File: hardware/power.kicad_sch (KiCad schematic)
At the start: 27 parts, among them J3 Battery, U9 MCP73811T-420I-OT

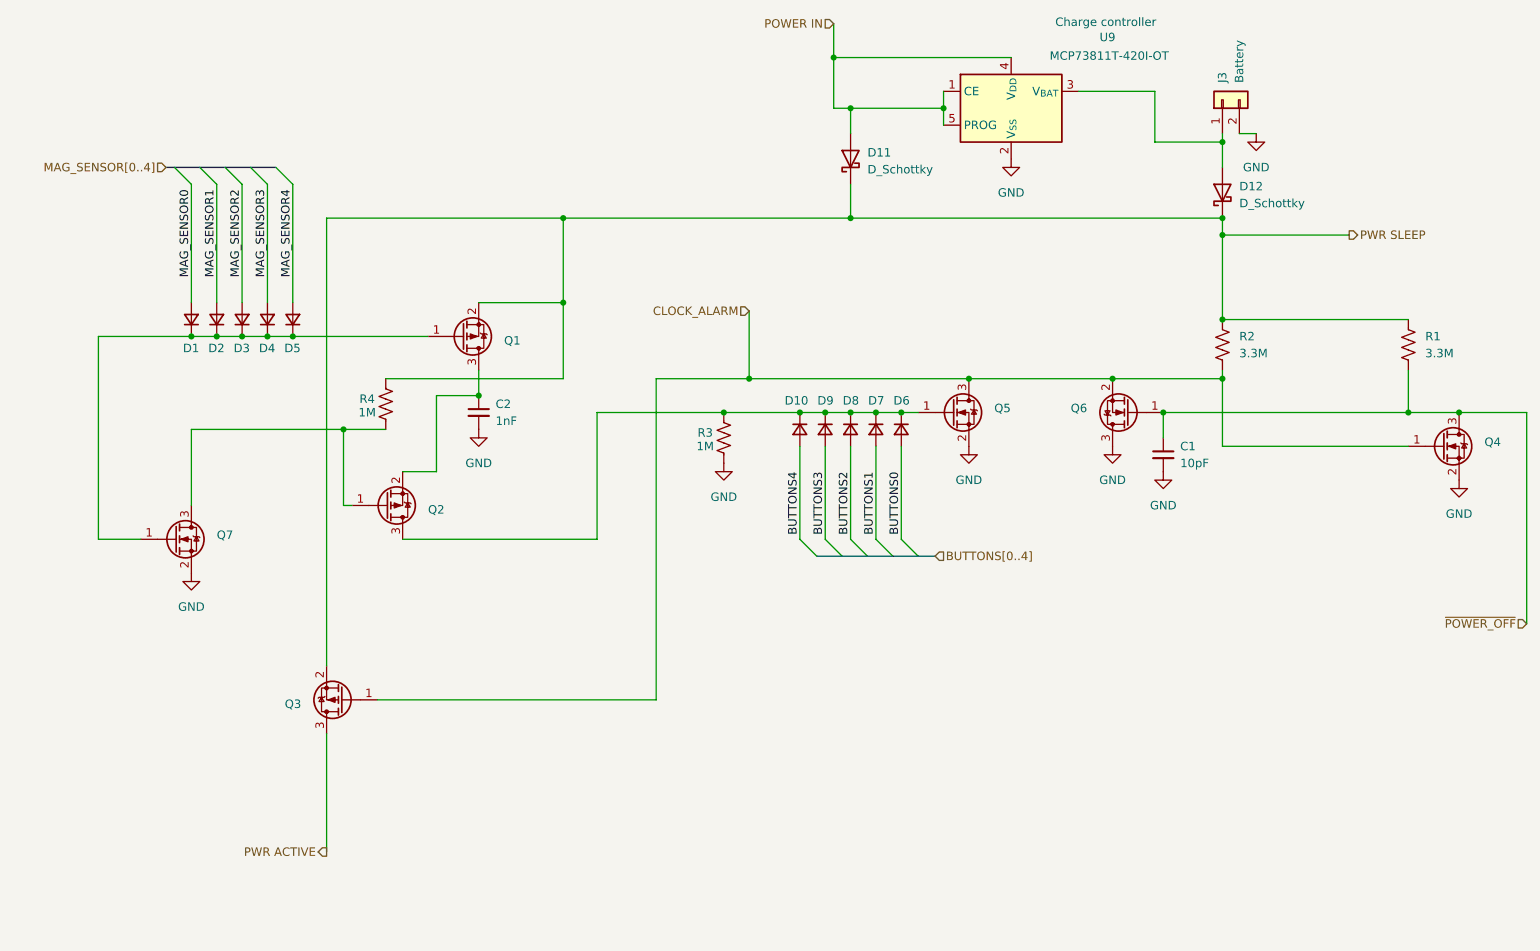
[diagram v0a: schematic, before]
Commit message: Schematic done
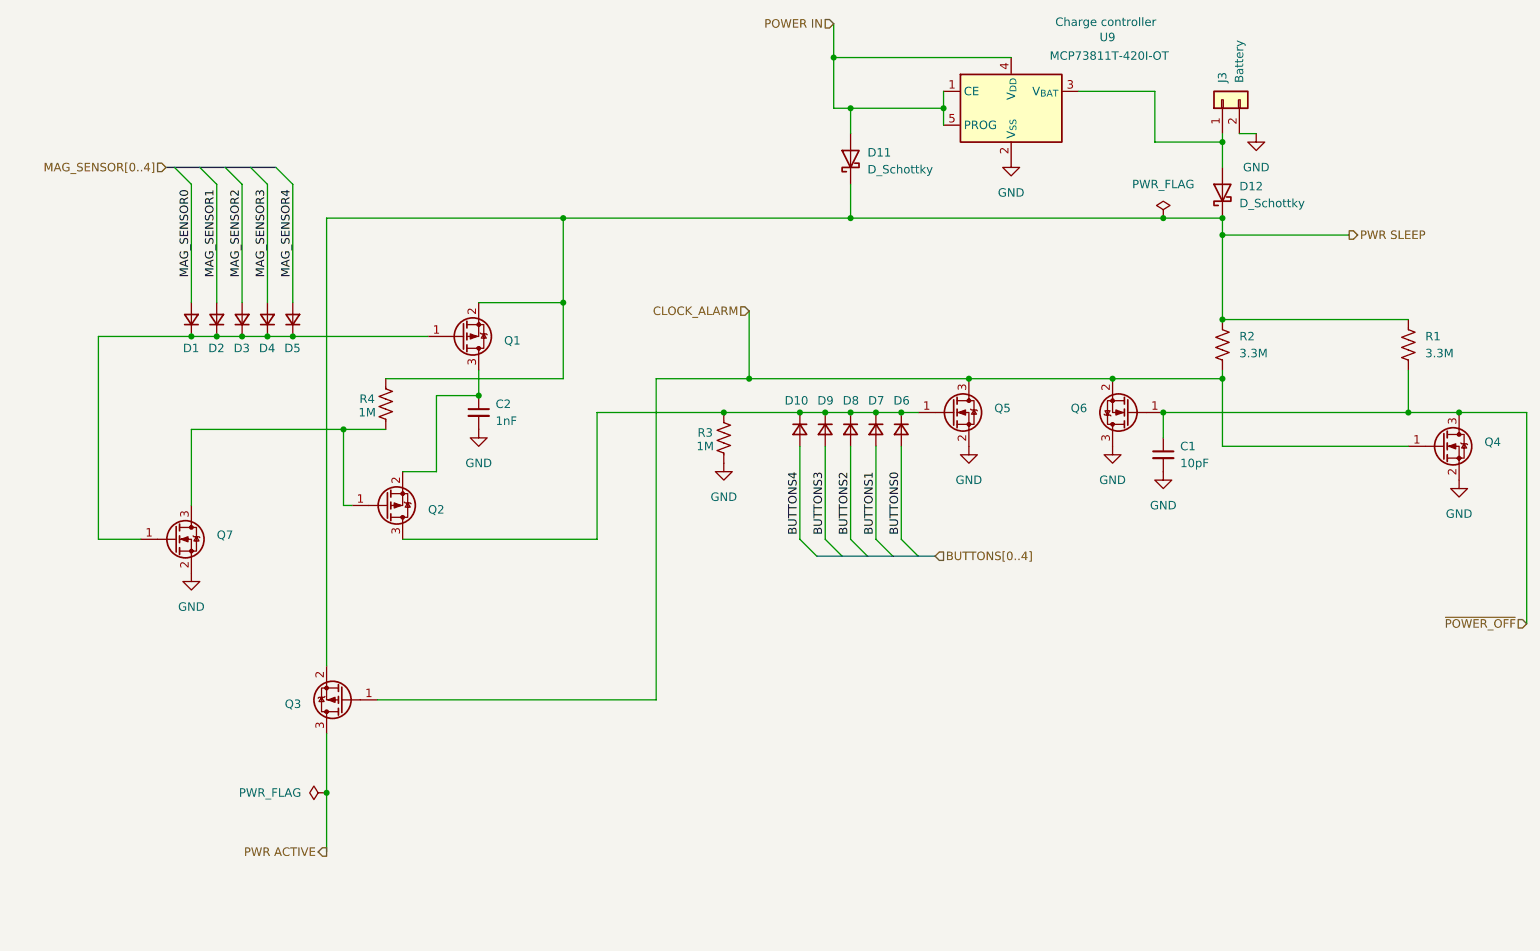
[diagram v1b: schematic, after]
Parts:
- R1, R2, R3, R4: footprint (none) -> Resistor_SMD:R_0402_1005Metric_Pad0.72x0.64mm_HandSolder
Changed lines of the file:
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@@
 	)
 	(junction
+		(at 73.66 132.08)
+		(diameter 0)
+		(color 0 0 0 0)
+	)
+	(junction
 		(at 208.28 48.26)
 		(diameter 0)
@@
 	)
 	(junction
+		(at 199.39 45.72)
+		(diameter 0)
+		(color 0 0 0 0)
+	)
+	(junction
 		(at 149.86 21.59)
 		(diameter 0)
@@
 	(wire
 		(pts
-			(xy 152.4 45.72) (xy 208.28 45.72)
+			(xy 152.4 45.72) (xy 199.39 45.72)
 		)
 		(stroke
@@
 	(wire
 		(pts
-			(xy 73.66 123.19) (xy 73.66 140.97)
+			(xy 73.66 123.19) (xy 73.66 132.08)
 		)
 		(stroke
@@
 	(wire
 		(pts
+			(xy 73.66 132.08) (xy 73.66 140.97)
+		)
+		(stroke
+			(width 0)
+			(type default)
+		)
+	)
+	(wire
+		(pts
 			(xy 149.86 29.21) (xy 152.4 29.21)
 		)
@@
 	(wire
 		(pts
+			(xy 199.39 45.72) (xy 208.28 45.72)
+		)
+		(stroke
+			(width 0)
+			(type default)
+		)
+	)
+	(wire
+		(pts
 			(xy 149.86 16.51) (xy 149.86 21.59)
 		)
@@
 			)
 		)
-		(property "Footprint" ""
+		(property "Footprint" "Resistor_SMD:R_0402_1005Metric_Pad0.72x0.64mm_HandSolder"
 			(at 209.296 65.024 90)
 			(effects
@@
 			)
 		)
-		(property "Footprint" ""
+		(property "Footprint" "Resistor_SMD:R_0402_1005Metric_Pad0.72x0.64mm_HandSolder"
 			(at 134.366 78.994 90)
 			(effects
@@
 			)
 		)
-		(property "Footprint" ""
+		(property "Footprint" "Resistor_SMD:R_0402_1005Metric_Pad0.72x0.64mm_HandSolder"
 			(at 83.566 73.914 90)
 			(effects
@@
 	)
 	(symbol
+		(lib_id "power:PWR_FLAG")
+		(at 199.39 45.72 0)
+		(unit 1)
+		(exclude_from_sim no)
+		(in_bom yes)
+		(on_board yes)
+		(dnp no)
+		(fields_autoplaced yes)
+		(property "Reference" "#FLG01"
+			(at 199.39 43.815 0)
+			(effects
+				(font
+					(size 1.27 1.27)
+				)
+				(hide yes)
+			)
+		)
+		(property "Value" "PWR_FLAG"
+			(at 199.39 40.64 0)
+			(effects
+				(font
+					(size 1.27 1.27)
+				)
+			)
+		)
+		(property "Footprint" ""
+			(at 199.39 45.72 0)
+			(effects
+				(font
+					(size 1.27 1.27)
+				)
+				(hide yes)
+			)
+		)
+		(property "Datasheet" "~"
+			(at 199.39 45.72 0)
+			(effects
+				(font
+					(size 1.27 1.27)
+				)
+				(hide yes)
+			)
+		)
+		(property "Description" "Special symbol for telling ERC where power comes from"
+			(at 199.39 45.72 0)
+			(effects
+				(font
+					(size 1.27 1.27)
+				)
+				(hide yes)
+			)
+		)
+		(pin "1"
+		)
+		(instances
+			(project ""
+				(path "/947839cd-c3fd-4edc-874b-58f50b880ae8/aa6729ee-32f9-4f43-8219-06c1c5d6987b"
+					(reference "#FLG01")
+					(unit 1)
+				)
+			)
+		)
+	)
+	(symbol
 		(lib_id "Device:D_Small")
 		(at 148.59 77.47 270)
@@
 			)
 		)
-		(property "Footprint" ""
+		(property "Footprint" "Resistor_SMD:R_0402_1005Metric_Pad0.72x0.64mm_HandSolder"
 			(at 237.236 65.024 90)
 			(effects
@@
 					(unit 1)
 				)
+			)
+		)
+	)
+	(symbol
+		(lib_id "power:PWR_FLAG")
+		(at 73.66 132.08 90)
+		(unit 1)
+		(exclude_from_sim no)
+		(in_bom yes)
+		(on_board yes)
+		(dnp no)
+		(fields_autoplaced yes)
+		(property "Reference" "#FLG02"
+			(at 71.755 132.08 0)
+			(effects
+				(font
+					(size 1.27 1.27)
+				)
+				(hide yes)
+			)
+		)
+		(property "Value" "PWR_FLAG"
+			(at 69.85 132.0799 90)
+			(effects
+				(font
+					(size 1.27 1.27)
+				)
+				(justify left)
+			)
+		)
+		(property "Footprint" ""
+			(at 73.66 132.08 0)
+			(effects
+				(font
+					(size 1.27 1.27)
+				)
+				(hide yes)
+			)
+		)
+		(property "Datasheet" "~"
+			(at 73.66 132.08 0)
+			(effects
+				(font
+					(size 1.27 1.27)
+				)
+				(hide yes)
+			)
+		)
+		(property "Description" "Special symbol for telling ERC where power comes from"
+			(at 73.66 132.08 0)
+			(effects
+				(font
+					(size 1.27 1.27)
+				)
+				(hide yes)
+			)
+		)
+		(pin "1"
+		)
+		(instances
+			(project "boombox"
+				(path "/947839cd-c3fd-4edc-874b-58f50b880ae8/aa6729ee-32f9-4f43-8219-06c1c5d6987b"
+					(reference "#FLG02")
+					(unit 1)
+				)

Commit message: values
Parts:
- added C17: 0.1uF, Capacitor_SMD:C_0402_1005Metric_Pad0.74x0.62mm_HandSolder, symbol Device:C_Small
- C2: footprint (none) -> Capacitor_SMD:C_0402_1005Metric_Pad0.74x0.62mm_HandSolder
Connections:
- net GND: now also C17.2
- net PWR SLEEP: now also C17.1
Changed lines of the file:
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@@
+	)
+	(symbol
+		(lib_id "Device:C_Small")
+		(at 152.4 48.26 0)
+		(unit 1)
+		(exclude_from_sim no)
+		(in_bom yes)
+		(on_board yes)
+		(dnp no)
+		(fields_autoplaced yes)
+		(property "Reference" "C17"
+			(at 154.94 46.9962 0)
+			(effects
+				(font
+					(size 1.27 1.27)
+				)
+				(justify left)
+			)
+		)
+		(property "Value" "0.1uF"
+			(at 154.94 49.5362 0)
+			(effects
+				(font
+					(size 1.27 1.27)
+				)
+				(justify left)
+			)
+		)
+		(property "Footprint" "Capacitor_SMD:C_0402_1005Metric_Pad0.74x0.62mm_HandSolder"
+			(at 152.4 48.26 0)
+			(effects
+				(font
+					(size 1.27 1.27)
+				)
+				(hide yes)
+			)
+		)
+		(property "Datasheet" "~"
+			(at 152.4 48.26 0)
+			(effects
+				(font
+					(size 1.27 1.27)
+				)
+				(hide yes)
+			)
+		)
+		(property "Description" "Unpolarized capacitor, small symbol"
+			(at 152.4 48.26 0)
+			(effects
+				(font
+					(size 1.27 1.27)
+				)
+				(hide yes)
+			)
+		)
+		(pin "1"
+		)
+		(pin "2"
+		)
+		(instances
+			(project "boombox"
+				(path "/947839cd-c3fd-4edc-874b-58f50b880ae8/aa6729ee-32f9-4f43-8219-06c1c5d6987b"
+					(reference "C17")
+					(unit 1)
+				)
+			)
+		)
 	)
 	(symbol
@@
 			)
 		)
-		(property "Footprint" ""
+		(property "Footprint" "Capacitor_SMD:C_0402_1005Metric_Pad0.74x0.62mm_HandSolder"
 			(at 96.52 74.93 0)
 			(effects
@@
 					(unit 1)
 				)
+			)
+		)
+	)
+	(symbol
+		(lib_id "power:GND")
+		(at 152.4 50.8 0)
+		(unit 1)
+		(exclude_from_sim no)
+		(in_bom yes)
+		(on_board yes)
+		(dnp no)
+		(property "Reference" "#PWR066"
+			(at 152.4 57.15 0)
+			(effects
+				(font
+					(size 1.27 1.27)
+				)
+				(hide yes)
+			)
+		)
+		(property "Value" "GND"
+			(at 152.4 55.88 0)
+			(effects
+				(font
+					(size 1.27 1.27)
+				)
+			)
+		)
+		(property "Footprint" ""
+			(at 152.4 50.8 0)
+			(effects
+				(font
+					(size 1.27 1.27)
+				)
+				(hide yes)
+			)
+		)
+		(property "Datasheet" ""
+			(at 152.4 50.8 0)
+			(effects
+				(font
+					(size 1.27 1.27)
+				)
+				(hide yes)
+			)
+		)
+		(property "Description" "Power symbol creates a global label with name \"GND\" , ground"
+			(at 152.4 50.8 0)
+			(effects
+				(font
+					(size 1.27 1.27)
+				)
+				(hide yes)
+			)
+		)
+		(pin "1"
+		)
+		(instances
+			(project "boombox"
+				(path "/947839cd-c3fd-4edc-874b-58f50b880ae8/aa6729ee-32f9-4f43-8219-06c1c5d6987b"
+					(reference "#PWR066")
+					(unit 1)
+				)

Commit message: Comitting so Nate can see errors
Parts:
- removed D1, D10, D2, D3, D4, D5, D6, D7, D8, D9: D_Small, symbol Device:D_Small
- added D1, D2, D3, D6, D7, D8: D_Dual_CommonCathode_AAK_Split, Package_TO_SOT_SMD:SOT-23-5, symbol Device:D_Dual_CommonCathode_AAK_Split
- C1: value 10pF -> 6pF; footprint (none) -> Capacitor_SMD:C_0402_1005Metric_Pad0.74x0.62mm_HandSolder
- D11, D12: footprint (none) -> Diode_SMD:D_SOD-123
- J3: footprint (none) -> boombox:Degson 3 Pin
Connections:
- net BUTTONS0: now also D8.1 (A)
- net BUTTONS1: now also D7.2 (A)
- net BUTTONS2: now also D7.1 (A)
- net BUTTONS3: now also D6.2 (A)
- net BUTTONS4: now also D6.1 (A)
- net MAG_SENSOR0: now also D3.1 (A)
- net MAG_SENSOR1: now also D2.2 (A)
- net MAG_SENSOR2: now also D2.1 (A)
- net MAG_SENSOR3: now also D1.2 (A)
- net MAG_SENSOR4: now also D1.1 (A)
- net at Q2.3 (D), Q5.1 (G), R3.1: now also D6.3 (K), D6.3 (K), D7.3 (K), D7.3 (K), D8.3 (K)
- net at Q1.1 (G), Q7.1 (G): now also D1.3 (K), D1.3 (K), D2.3 (K), D2.3 (K), D3.3 (K)
- no-connect marks 0 -> 4

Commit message: Routing
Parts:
- D1, D2, D3, D6, D7, D8: footprint Package_TO_SOT_SMD:SOT-23-5 -> Package_TO_SOT_SMD:SOT-23
- J3: footprint boombox:Degson 3 Pin -> boombox:EBAA02C
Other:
- moved on the sheet: Q7
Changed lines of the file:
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@@
 	(wire
 		(pts
-			(xy 39.37 93.98) (xy 45.72 93.98)
+			(xy 39.37 82.55) (xy 50.8 82.55)
 		)
 		(stroke
@@
 	(wire
 		(pts
-			(xy 53.34 77.47) (xy 53.34 88.9)
-		)
-		(stroke
-			(width 0)
-			(type default)
-		)
-	)
-	(wire
-		(pts
 			(xy 76.2 77.47) (xy 76.2 88.9)
 		)
@@
 	(wire
 		(pts
+			(xy 58.42 87.63) (xy 58.42 90.17)
+		)
+		(stroke
+			(width 0)
+			(type default)
+		)
+	)
+	(wire
+		(pts
 			(xy 152.4 40.64) (xy 152.4 45.72)
 		)
@@
 	(wire
 		(pts
-			(xy 76.2 77.47) (xy 53.34 77.47)
+			(xy 76.2 77.47) (xy 58.42 77.47)
 		)
 		(stroke
@@
 	(wire
 		(pts
-			(xy 39.37 63.5) (xy 39.37 93.98)
+			(xy 39.37 63.5) (xy 39.37 82.55)
 		)
 		(stroke
@@
 	(symbol
 		(lib_id "power:GND")
-		(at 53.34 99.06 0)
+		(at 58.42 90.17 0)
 		(unit 1)
 		(exclude_from_sim no)
@@
 		(dnp no)
 		(property "Reference" "#PWR018"
-			(at 53.34 105.41 0)
+			(at 58.42 96.52 0)
 			(effects
 				(font
@@
 		)
 		(property "Value" "GND"
-			(at 53.34 104.14 0)
+			(at 58.42 95.25 0)
 			(effects
 				(font
@@
 		)
 		(property "Footprint" ""
-			(at 53.34 99.06 0)
+			(at 58.42 90.17 0)
 			(effects
 				(font
@@
 		)
 		(property "Datasheet" ""
-			(at 53.34 99.06 0)
+			(at 58.42 90.17 0)
 			(effects
 				(font
@@
 		)
 		(property "Description" "Power symbol creates a global label with name \"GND\" , ground"
-			(at 53.34 99.06 0)
+			(at 58.42 90.17 0)
 			(effects
 				(font
@@
 			)
 		)
-		(property "Footprint" "Package_TO_SOT_SMD:SOT-23-5"
+		(property "Footprint" "Package_TO_SOT_SMD:SOT-23"
 			(at 66.04 57.15 0)
 			(effects
@@
 			)
 		)
-		(property "Footprint" "Package_TO_SOT_SMD:SOT-23-5"
+		(property "Footprint" "Package_TO_SOT_SMD:SOT-23"
 			(at 62.23 57.15 0)
 			(effects
@@
 			)
 		)
-		(property "Footprint" "Package_TO_SOT_SMD:SOT-23-5"
+		(property "Footprint" "Package_TO_SOT_SMD:SOT-23"
 			(at 154.94 81.28 0)
 			(effects
@@
 			)
 		)
-		(property "Footprint" "Package_TO_SOT_SMD:SOT-23-5"
+		(property "Footprint" "Package_TO_SOT_SMD:SOT-23"
 			(at 58.42 57.15 0)
 			(effects
@@
 			)
 		)
-		(property "Footprint" "Package_TO_SOT_SMD:SOT-23-5"
+		(property "Footprint" "Package_TO_SOT_SMD:SOT-23"
 			(at 162.56 81.28 0)
 			(effects
@@
 	(symbol
 		(lib_id "boombox:DMN2310U-7")
-		(at 52.07 93.98 0)
+		(at 57.15 82.55 0)
 		(unit 1)
 		(exclude_from_sim no)
@@
 		(dnp no)
 		(property "Reference" "Q7"
-			(at 57.15 93.3449 0)
+			(at 62.23 81.9149 0)
 			(effects
 				(font
@@
 		)
 		(property "Value" "~"
-			(at 57.15 95.25 0)
+			(at 62.23 83.82 0)
 			(effects
 				(font
@@
 		)
 		(property "Footprint" "Package_TO_SOT_SMD:SOT-23"
-			(at 53.34 108.458 0)
+			(at 58.42 97.028 0)
 			(effects
 				(font
@@
 		)
 		(property "Datasheet" ""
-			(at 52.07 93.98 0)
+			(at 57.15 82.55 0)
 			(effects
 				(font
@@
 		)
 		(property "Description" ""
-			(at 52.07 93.98 0)
+			(at 57.15 82.55 0)
 			(effects
 				(font
@@
 		)
 		(property "Sim.Device" ""
-			(at 52.07 93.98 0)
+			(at 57.15 82.55 0)
 			(effects
 				(font
@@
 		)
 		(property "Sim.Pins" ""
-			(at 52.07 93.98 0)
+			(at 57.15 82.55 0)
 			(effects
 				(font
@@
 			)
 		)
-		(property "Footprint" "Package_TO_SOT_SMD:SOT-23-5"
+		(property "Footprint" "Package_TO_SOT_SMD:SOT-23"
 			(at 147.32 81.28 0)
 			(effects
@@
 			)
 		)
-		(property "Footprint" "boombox:Degson 3 Pin"
+		(property "Footprint" "boombox:EBAA02C"
 			(at 208.28 27.94 0)
 			(effects
@@
 			)
 		)
-		(property "Footprint" "Package_TO_SOT_SMD:SOT-23-5"
+		(property "Footprint" "Package_TO_SOT_SMD:SOT-23"
 			(at 158.75 81.28 0)
 			(effects
@@
 			)
 		)
-		(property "Footprint" "Package_TO_SOT_SMD:SOT-23-5"
+		(property "Footprint" "Package_TO_SOT_SMD:SOT-23"
 			(at 128.27 139.7 0)
 			(effects
@@
 			)
 		)
-		(property "Footprint" "Package_TO_SOT_SMD:SOT-23-5"
+		(property "Footprint" "Package_TO_SOT_SMD:SOT-23"
 			(at 54.61 57.15 0)
 			(effects
@@
 			)
 		)
-		(property "Footprint" "Package_TO_SOT_SMD:SOT-23-5"
+		(property "Footprint" "Package_TO_SOT_SMD:SOT-23"
 			(at 151.13 81.28 0)
 			(effects
@@
 			)
 		)
-		(property "Footprint" "Package_TO_SOT_SMD:SOT-23-5"
+		(property "Footprint" "Package_TO_SOT_SMD:SOT-23"
 			(at 128.27 149.86 0)
 			(effects
@@
 			)
 		)
-		(property "Footprint" "Package_TO_SOT_SMD:SOT-23-5"
+		(property "Footprint" "Package_TO_SOT_SMD:SOT-23"
 			(at 50.8 57.15 0)
 			(effects

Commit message: Switches
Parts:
- added R5: 1M, Resistor_SMD:R_0402_1005Metric_Pad0.72x0.64mm_HandSolder, symbol Device:R_US
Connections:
- net GND: now also R5.2
- net at D1.3 (K), D1.3 (K), D2.3 (K)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: now also R5.1
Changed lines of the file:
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@@
 	)
 	(junction
+		(at 45.72 63.5)
+		(diameter 0)
+		(color 0 0 0 0)
+	)
+	(junction
 		(at 199.39 45.72)
 		(diameter 0)
@@
 	(wire
 		(pts
-			(xy 39.37 63.5) (xy 53.34 63.5)
+			(xy 39.37 63.5) (xy 45.72 63.5)
 		)
 		(stroke
@@
 	(wire
 		(pts
+			(xy 45.72 63.5) (xy 53.34 63.5)
+		)
+		(stroke
+			(width 0)
+			(type default)
+		)
+	)
+	(wire
+		(pts
 			(xy 96.52 58.42) (xy 109.22 58.42)
 		)
@@
 	)
 	(symbol
+		(lib_id "Device:R_US")
+		(at 45.72 67.31 0)
+		(unit 1)
+		(exclude_from_sim no)
+		(in_bom yes)
+		(on_board yes)
+		(dnp no)
+		(property "Reference" "R5"
+			(at 42.926 66.548 0)
+			(effects
+				(font
+					(size 1.27 1.27)
+				)
+			)
+		)
+		(property "Value" "1M"
+			(at 42.926 68.58 0)
+			(effects
+				(font
+					(size 1.27 1.27)
+				)
+			)
+		)
+		(property "Footprint" "Resistor_SMD:R_0402_1005Metric_Pad0.72x0.64mm_HandSolder"
+			(at 46.736 67.564 90)
+			(effects
+				(font
+					(size 1.27 1.27)
+				)
+				(hide yes)
+			)
+		)
+		(property "Datasheet" "~"
+			(at 45.72 67.31 0)
+			(effects
+				(font
+					(size 1.27 1.27)
+				)
+				(hide yes)
+			)
+		)
+		(property "Description" "Resistor, US symbol"
+			(at 45.72 67.31 0)
+			(effects
+				(font
+					(size 1.27 1.27)
+				)
+				(hide yes)
+			)
+		)
+		(property "Sim.Device" ""
+			(at 45.72 67.31 0)
+			(effects
+				(font
+					(size 1.27 1.27)
+				)
+				(hide yes)
+			)
+		)
+		(property "Sim.Pins" ""
+			(at 45.72 67.31 0)
+			(effects
+				(font
+					(size 1.27 1.27)
+				)
+				(hide yes)
+			)
+		)
+		(pin "2"
+		)
+		(pin "1"
+		)
+		(instances
+			(project "boombox"
+				(path "/947839cd-c3fd-4edc-874b-58f50b880ae8/aa6729ee-32f9-4f43-8219-06c1c5d6987b"
+					(reference "R5")
+					(unit 1)
+				)
+			)
+		)
+	)
+	(symbol
 		(lib_id "Device:D_Schottky")
 		(at 208.28 41.91 90)
@@
 					(unit 1)
 				)
+			)
+		)
+	)
+	(symbol
+		(lib_id "power:GND")
+		(at 45.72 71.12 0)
+		(unit 1)
+		(exclude_from_sim no)
+		(in_bom yes)
+		(on_board yes)
+		(dnp no)
+		(property "Reference" "#PWR06"
+			(at 45.72 77.47 0)
+			(effects
+				(font
+					(size 1.27 1.27)
+				)
+				(hide yes)
+			)
+		)
+		(property "Value" "GND"
+			(at 45.72 76.2 0)
+			(effects
+				(font
+					(size 1.27 1.27)
+				)
+			)
+		)
+		(property "Footprint" ""
+			(at 45.72 71.12 0)
+			(effects
+				(font
+					(size 1.27 1.27)
+				)
+				(hide yes)
+			)
+		)
+		(property "Datasheet" ""
+			(at 45.72 71.12 0)
+			(effects
+				(font
+					(size 1.27 1.27)
+				)
+				(hide yes)
+			)
+		)
+		(property "Description" "Power symbol creates a global label with name \"GND\" , ground"
+			(at 45.72 71.12 0)
+			(effects
+				(font
+					(size 1.27 1.27)
+				)
+				(hide yes)
+			)
+		)
+		(pin "1"
+		)
+		(instances
+			(project "boombox"
+				(path "/947839cd-c3fd-4edc-874b-58f50b880ae8/aa6729ee-32f9-4f43-8219-06c1c5d6987b"
+					(reference "#PWR06")
+					(unit 1)
+				)
